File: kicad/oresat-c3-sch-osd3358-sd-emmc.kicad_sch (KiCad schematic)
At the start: 41 parts, among them J5 DM3BT-DSF-PEJS, U1 OSD3358-512M-BSM, U8 TCAN330, U9 EMMC+RESET+5.1-COMPATIBLE-BA

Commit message: Fixed test points; added RF test points. Started on layout and component packages for UHF radio.
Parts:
- TP23, TP24, TP26, TP27, TP31, TP32, TP37, TP38, TP39, TP40, TP42, TP46, TP47, TP48, TP49, TP50: footprint TestPoint:TestPoint_Pad_D1.0mm -> oresat-misc:TestPoint_Pad_D1.0mm
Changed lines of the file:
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@@
       (effects (font (size 1.27 1.27)) hide)
     )
-    (property "Footprint" "TestPoint:TestPoint_Pad_D1.0mm" (at 160.02 93.98 0)
+    (property "Footprint" "oresat-misc:TestPoint_Pad_D1.0mm" (at 160.02 93.98 0)
       (effects (font (size 1.27 1.27)) hide)
     )
@@
       (effects (font (size 1.27 1.27)) hide)
     )
-    (property "Footprint" "TestPoint:TestPoint_Pad_D1.0mm" (at 228.6 119.38 0)
+    (property "Footprint" "oresat-misc:TestPoint_Pad_D1.0mm" (at 228.6 119.38 0)
       (effects (font (size 1.27 1.27)) hide)
     )
@@
       (effects (font (size 1.27 1.27)) hide)
     )
-    (property "Footprint" "TestPoint:TestPoint_Pad_D1.0mm" (at 228.6 154.94 0)
+    (property "Footprint" "oresat-misc:TestPoint_Pad_D1.0mm" (at 228.6 154.94 0)
       (effects (font (size 1.27 1.27)) hide)
     )
@@
       (effects (font (size 1.27 1.27)) hide)
     )
-    (property "Footprint" "TestPoint:TestPoint_Pad_D1.0mm" (at 228.6 116.84 0)
+    (property "Footprint" "oresat-misc:TestPoint_Pad_D1.0mm" (at 228.6 116.84 0)
       (effects (font (size 1.27 1.27)) hide)
     )
@@
       (effects (font (size 1.27 1.27)) hide)
     )
-    (property "Footprint" "TestPoint:TestPoint_Pad_D1.0mm" (at 228.6 198.12 0)
+    (property "Footprint" "oresat-misc:TestPoint_Pad_D1.0mm" (at 228.6 198.12 0)
       (effects (font (size 1.27 1.27)) hide)
     )
@@
       (effects (font (size 1.27 1.27)) hide)
     )
-    (property "Footprint" "TestPoint:TestPoint_Pad_D1.0mm" (at 144.78 59.69 0)
+    (property "Footprint" "oresat-misc:TestPoint_Pad_D1.0mm" (at 144.78 59.69 0)
       (effects (font (size 1.27 1.27)) hide)
     )
@@
       (effects (font (size 1.27 1.27)) hide)
     )
-    (property "Footprint" "TestPoint:TestPoint_Pad_D1.0mm" (at 228.6 124.46 0)
+    (property "Footprint" "oresat-misc:TestPoint_Pad_D1.0mm" (at 228.6 124.46 0)
       (effects (font (size 1.27 1.27)) hide)
     )
@@
       (effects (font (size 1.27 1.27)) hide)
     )
-    (property "Footprint" "TestPoint:TestPoint_Pad_D1.0mm" (at 228.6 195.58 0)
+    (property "Footprint" "oresat-misc:TestPoint_Pad_D1.0mm" (at 228.6 195.58 0)
       (effects (font (size 1.27 1.27)) hide)
     )
@@
       (effects (font (size 1.27 1.27)) hide)
     )
-    (property "Footprint" "TestPoint:TestPoint_Pad_D1.0mm" (at 228.6 167.64 0)
+    (property "Footprint" "oresat-misc:TestPoint_Pad_D1.0mm" (at 228.6 167.64 0)
       (effects (font (size 1.27 1.27)) hide)
     )
@@
       (effects (font (size 1.27 1.27)) hide)
     )
-    (property "Footprint" "TestPoint:TestPoint_Pad_D1.0mm" (at 160.02 172.72 0)
+    (property "Footprint" "oresat-misc:TestPoint_Pad_D1.0mm" (at 160.02 172.72 0)
       (effects (font (size 1.27 1.27)) hide)
     )
@@
       (effects (font (size 1.27 1.27)) hide)
     )
-    (property "Footprint" "TestPoint:TestPoint_Pad_D1.0mm" (at 228.6 160.02 0)
+    (property "Footprint" "oresat-misc:TestPoint_Pad_D1.0mm" (at 228.6 160.02 0)
       (effects (font (size 1.27 1.27)) hide)
     )
@@
       (effects (font (size 1.27 1.27)) hide)
     )
-    (property "Footprint" "TestPoint:TestPoint_Pad_D1.0mm" (at 228.6 121.92 0)
+    (property "Footprint" "oresat-misc:TestPoint_Pad_D1.0mm" (at 228.6 121.92 0)
       (effects (font (size 1.27 1.27)) hide)
     )
@@
       (effects (font (size 1.27 1.27)) hide)
     )
-    (property "Footprint" "TestPoint:TestPoint_Pad_D1.0mm" (at 160.02 111.76 0)
+    (property "Footprint" "oresat-misc:TestPoint_Pad_D1.0mm" (at 160.02 111.76 0)
       (effects (font (size 1.27 1.27)) hide)
     )
@@
       (effects (font (size 1.27 1.27)) hide)
     )
-    (property "Footprint" "TestPoint:TestPoint_Pad_D1.0mm" (at 144.78 62.23 0)
+    (property "Footprint" "oresat-misc:TestPoint_Pad_D1.0mm" (at 144.78 62.23 0)
       (effects (font (size 1.27 1.27)) hide)
     )
@@
       (effects (font (size 1.27 1.27)) hide)
     )
-    (property "Footprint" "TestPoint:TestPoint_Pad_D1.0mm" (at 228.6 142.24 0)
+    (property "Footprint" "oresat-misc:TestPoint_Pad_D1.0mm" (at 228.6 142.24 0)
       (effects (font (size 1.27 1.27)) hide)
     )
@@
       (effects (font (size 1.27 1.27)) hide)
     )
-    (property "Footprint" "TestPoint:TestPoint_Pad_D1.0mm" (at 160.02 175.26 0)
-      (effects (font (size 1.27 1.27)) hide)
-    )
+    (property "Footprint" "oresat-misc:TestPoint_Pad_D1.0mm" (at 160.02 175.26 0)
+      (effects (font (size 1.27 1.27)) hide)
+    )

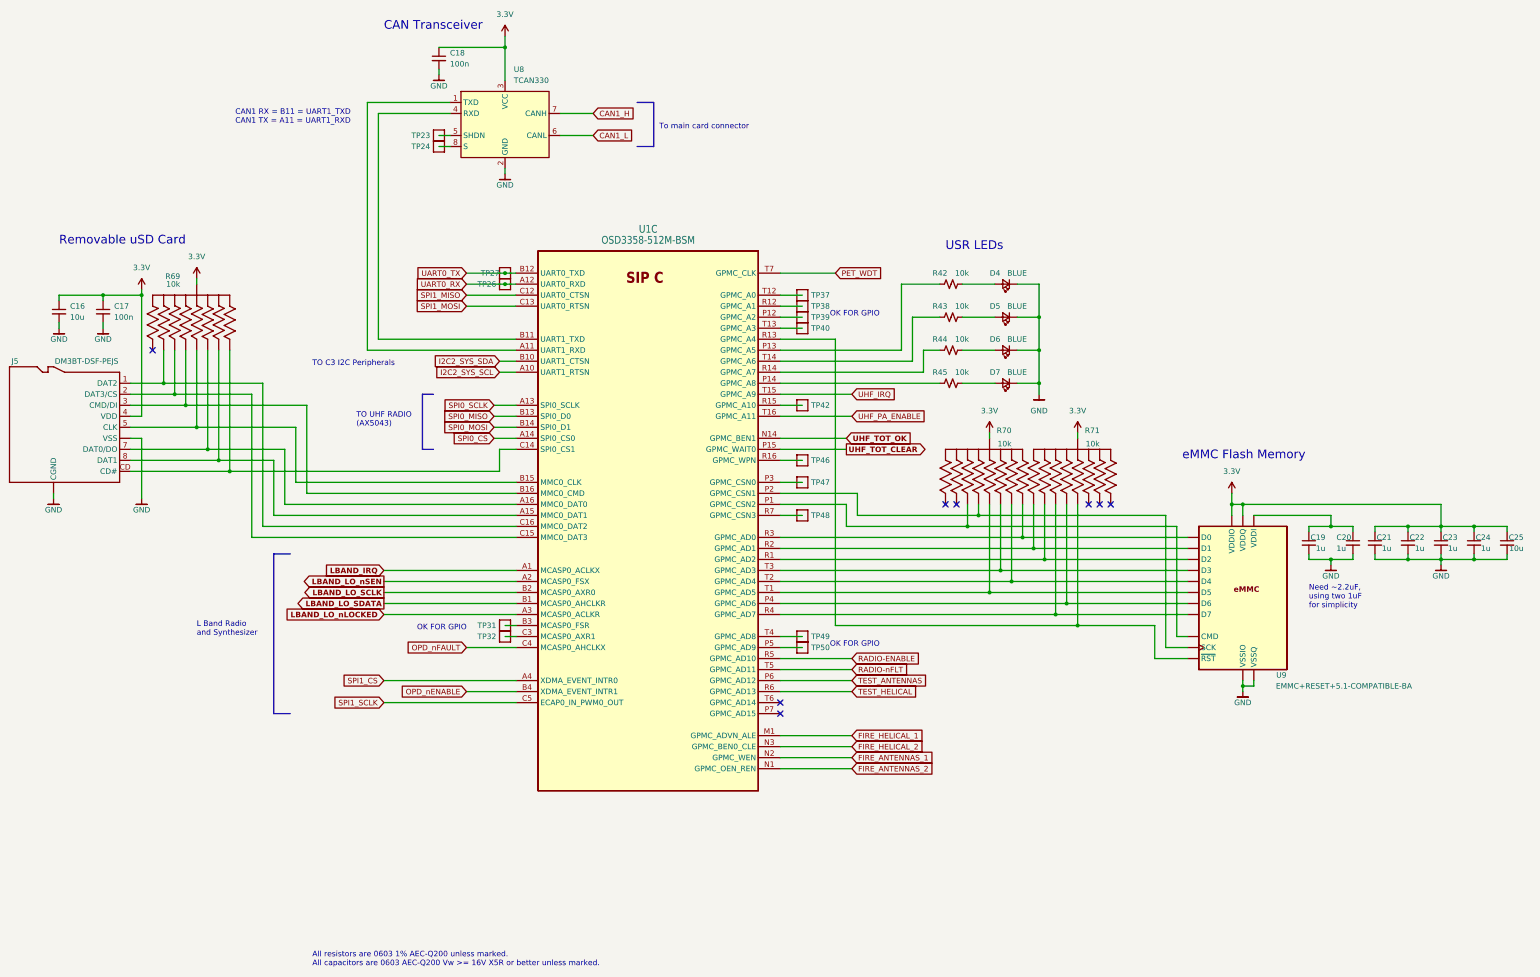
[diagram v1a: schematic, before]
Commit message: Fixed footprints and laid out WDT and OPD circuitry.
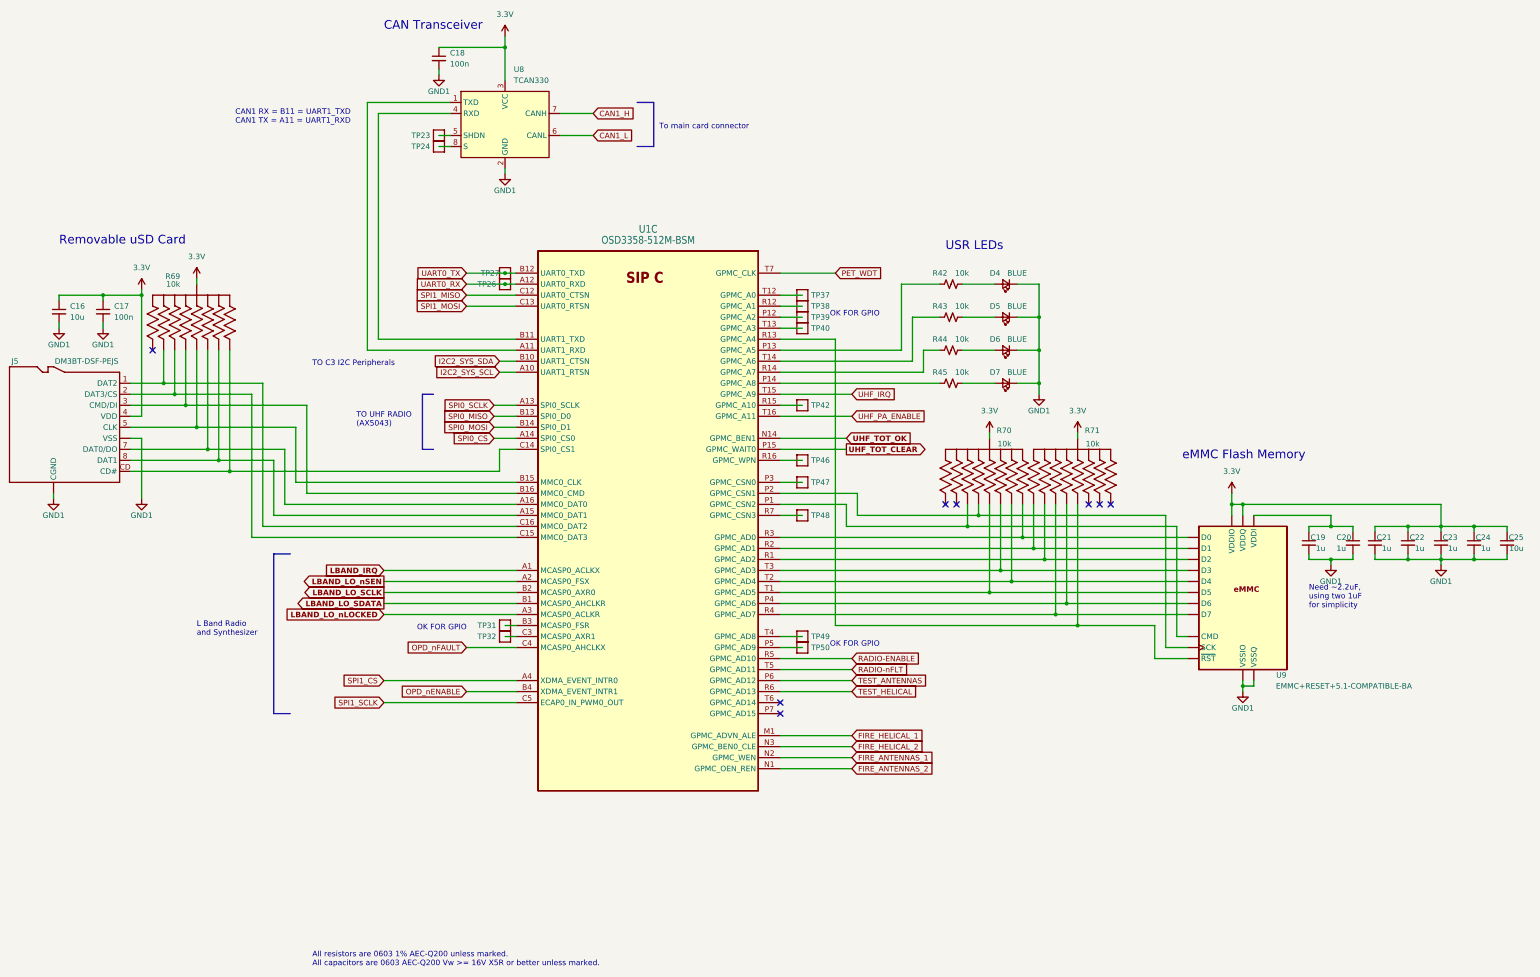
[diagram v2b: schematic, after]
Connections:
- net GND renamed GND1
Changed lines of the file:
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@@
     )
   )
-  (symbol (lib_id "oresat-power:GND") (at 375.92 168.91 0) (unit 1)
-    (in_bom yes) (on_board yes) (dnp no)
-    (property "Reference" "#GND0147" (at 375.92 175.26 0)
-      (effects (font (size 1.27 1.27)) hide)
-    )
-    (property "Value" "GND" (at 375.92 171.45 0)
+  (symbol (lib_id "power:GND1") (at 375.92 168.91 0) (unit 1)
+    (in_bom yes) (on_board yes) (dnp no)
+    (property "Reference" "#PWR0149" (at 375.92 175.26 0)
+      (effects (font (size 1.27 1.27)) hide)
+    )
+    (property "Value" "GND1" (at 375.92 172.72 0)
       (effects (font (size 1.27 1.27)))
     )
@@
       (project "oresat-c3"
         (path "/65d12cdd-c326-4033-9053-c59fa4e0b25e/f3d147ad-4cea-4d77-ae60-95882b03454e"
-          (reference "#GND0147") (unit 1)
+          (reference "#PWR0149") (unit 1)
         )
       )
@@
     )
   )
-  (symbol (lib_id "oresat-power:GND") (at 55.88 153.67 0) (unit 1)
-    (in_bom yes) (on_board yes) (dnp no)
-    (property "Reference" "#GND0138" (at 55.88 160.02 0)
-      (effects (font (size 1.27 1.27)) hide)
-    )
-    (property "Value" "GND" (at 55.88 156.21 0)
+  (symbol (lib_id "power:GND1") (at 55.88 153.67 0) (unit 1)
+    (in_bom yes) (on_board yes) (dnp no)
+    (property "Reference" "#PWR0155" (at 55.88 160.02 0)
+      (effects (font (size 1.27 1.27)) hide)
+    )
+    (property "Value" "GND1" (at 55.88 157.48 0)
       (effects (font (size 1.27 1.27)))
     )
@@
       (project "oresat-c3"
         (path "/65d12cdd-c326-4033-9053-c59fa4e0b25e/f3d147ad-4cea-4d77-ae60-95882b03454e"
-          (reference "#GND0138") (unit 1)
+          (reference "#PWR0155") (unit 1)
         )
       )
@@
     )
   )
-  (symbol (lib_id "oresat-power:GND") (at 283.21 129.54 0) (unit 1)
+  (symbol (lib_id "power:GND1") (at 283.21 129.54 0) (unit 1)
     (in_bom yes) (on_board yes) (dnp no) (fields_autoplaced)
-    (property "Reference" "#GND0150" (at 283.21 135.89 0)
-      (effects (font (size 1.27 1.27)) hide)
-    )
-    (property "Value" "GND" (at 283.21 133.35 0)
+    (property "Reference" "#PWR0148" (at 283.21 135.89 0)
+      (effects (font (size 1.27 1.27)) hide)
+    )
+    (property "Value" "GND1" (at 283.21 133.35 0)
       (effects (font (size 1.27 1.27)))
     )
@@
       (project "oresat-c3"
         (path "/65d12cdd-c326-4033-9053-c59fa4e0b25e/f3d147ad-4cea-4d77-ae60-95882b03454e"
-          (reference "#GND0150") (unit 1)
-        )
-      )
-    )
-  )
-  (symbol (lib_id "oresat-power:GND") (at 76.2 153.67 0) (unit 1)
-    (in_bom yes) (on_board yes) (dnp no)
-    (property "Reference" "#GND0139" (at 76.2 160.02 0)
-      (effects (font (size 1.27 1.27)) hide)
-    )
-    (property "Value" "GND" (at 76.2 156.21 0)
+          (reference "#PWR0148") (unit 1)
+        )
+      )
+    )
+  )
+  (symbol (lib_id "power:GND1") (at 76.2 153.67 0) (unit 1)
+    (in_bom yes) (on_board yes) (dnp no)
+    (property "Reference" "#PWR0156" (at 76.2 160.02 0)
+      (effects (font (size 1.27 1.27)) hide)
+    )
+    (property "Value" "GND1" (at 76.2 157.48 0)
       (effects (font (size 1.27 1.27)))
     )
@@
       (project "oresat-c3"
         (path "/65d12cdd-c326-4033-9053-c59fa4e0b25e/f3d147ad-4cea-4d77-ae60-95882b03454e"
-          (reference "#GND0139") (unit 1)
+          (reference "#PWR0156") (unit 1)
         )
       )
@@
     )
   )
-  (symbol (lib_id "oresat-power:GND") (at 350.52 168.91 0) (unit 1)
-    (in_bom yes) (on_board yes) (dnp no)
-    (property "Reference" "#GND0149" (at 350.52 175.26 0)
-      (effects (font (size 1.27 1.27)) hide)
-    )
-    (property "Value" "GND" (at 350.52 171.45 0)
+  (symbol (lib_id "power:GND1") (at 350.52 168.91 0) (unit 1)
+    (in_bom yes) (on_board yes) (dnp no)
+    (property "Reference" "#PWR0151" (at 350.52 175.26 0)
+      (effects (font (size 1.27 1.27)) hide)
+    )
+    (property "Value" "GND1" (at 350.52 172.72 0)
       (effects (font (size 1.27 1.27)))
     )
@@
       (project "oresat-c3"
         (path "/65d12cdd-c326-4033-9053-c59fa4e0b25e/f3d147ad-4cea-4d77-ae60-95882b03454e"
-          (reference "#GND0149") (unit 1)
-        )
-      )
-    )
-  )
-  (symbol (lib_id "oresat-power:GND") (at 57.15 114.3 0) (unit 1)
-    (in_bom yes) (on_board yes) (dnp no)
-    (property "Reference" "#GND0140" (at 57.15 120.65 0)
-      (effects (font (size 1.27 1.27)) hide)
-    )
-    (property "Value" "GND" (at 57.15 116.84 0)
+          (reference "#PWR0151") (unit 1)
+        )
+      )
+    )
+  )
+  (symbol (lib_id "power:GND1") (at 57.15 114.3 0) (unit 1)
+    (in_bom yes) (on_board yes) (dnp no)
+    (property "Reference" "#PWR0152" (at 57.15 120.65 0)
+      (effects (font (size 1.27 1.27)) hide)
+    )
+    (property "Value" "GND1" (at 57.15 118.11 0)
       (effects (font (size 1.27 1.27)))
     )
@@
       (project "oresat-c3"
         (path "/65d12cdd-c326-4033-9053-c59fa4e0b25e/f3d147ad-4cea-4d77-ae60-95882b03454e"
-          (reference "#GND0140") (unit 1)
+          (reference "#PWR0152") (unit 1)
         )
       )
@@
     )
   )
-  (symbol (lib_id "oresat-power:GND") (at 67.31 114.3 0) (unit 1)
-    (in_bom yes) (on_board yes) (dnp no)
-    (property "Reference" "#GND0141" (at 67.31 120.65 0)
-      (effects (font (size 1.27 1.27)) hide)
-    )
-    (property "Value" "GND" (at 67.31 116.84 0)
+  (symbol (lib_id "power:GND1") (at 67.31 114.3 0) (unit 1)
+    (in_bom yes) (on_board yes) (dnp no)
+    (property "Reference" "#PWR0153" (at 67.31 120.65 0)
+      (effects (font (size 1.27 1.27)) hide)
+    )
+    (property "Value" "GND1" (at 67.31 118.11 0)
       (effects (font (size 1.27 1.27)))
     )
@@
       (project "oresat-c3"
         (path "/65d12cdd-c326-4033-9053-c59fa4e0b25e/f3d147ad-4cea-4d77-ae60-95882b03454e"
-          (reference "#GND0141") (unit 1)
+          (reference "#PWR0153") (unit 1)
         )
       )
@@
     )
   )
-  (symbol (lib_id "oresat-power:GND") (at 160.02 78.74 0) (unit 1)
-    (in_bom yes) (on_board yes) (dnp no)
-    (property "Reference" "#GND0146" (at 160.02 85.09 0)
-      (effects (font (size 1.27 1.27)) hide)
-    )
-    (property "Value" "GND" (at 160.02 81.28 0)
+  (symbol (lib_id "power:GND1") (at 160.02 78.74 0) (unit 1)
+    (in_bom yes) (on_board yes) (dnp no)
+    (property "Reference" "#PWR0157" (at 160.02 85.09 0)
+      (effects (font (size 1.27 1.27)) hide)
+    )
+    (property "Value" "GND1" (at 160.02 82.55 0)
       (effects (font (size 1.27 1.27)))
     )
@@
       (project "oresat-c3"
         (path "/65d12cdd-c326-4033-9053-c59fa4e0b25e/f3d147ad-4cea-4d77-ae60-95882b03454e"
-          (reference "#GND0146") (unit 1)
+          (reference "#PWR0157") (unit 1)
         )
       )
@@
     )
   )
-  (symbol (lib_id "oresat-power:GND") (at 330.2 198.12 0) (unit 1)
-    (in_bom yes) (on_board yes) (dnp no)
-    (property "Reference" "#GND0148" (at 330.2 204.47 0)
-      (effects (font (size 1.27 1.27)) hide)
-    )
-    (property "Value" "GND" (at 330.2 200.66 0)
+  (symbol (lib_id "power:GND1") (at 330.2 198.12 0) (unit 1)
+    (in_bom yes) (on_board yes) (dnp no)
+    (property "Reference" "#PWR0150" (at 330.2 204.47 0)
+      (effects (font (size 1.27 1.27)) hide)
+    )
+    (property "Value" "GND1" (at 330.2 201.93 0)
       (effects (font (size 1.27 1.27)))
     )
@@
       (project "oresat-c3"
         (path "/65d12cdd-c326-4033-9053-c59fa4e0b25e/f3d147ad-4cea-4d77-ae60-95882b03454e"
-          (reference "#GND0148") (unit 1)
-        )
-      )
-    )
-  )
-  (symbol (lib_id "oresat-power:GND") (at 144.78 55.88 0) (unit 1)
-    (in_bom yes) (on_board yes) (dnp no)
-    (property "Reference" "#GND0145" (at 144.78 62.23 0)
-      (effects (font (size 1.27 1.27)) hide)
-    )
-    (property "Value" "GND" (at 144.78 58.42 0)
+          (reference "#PWR0150") (unit 1)
+        )
+      )
+    )
+  )
+  (symbol (lib_id "power:GND1") (at 144.78 55.88 0) (unit 1)
+    (in_bom yes) (on_board yes) (dnp no)
+    (property "Reference" "#PWR0154" (at 144.78 62.23 0)
+      (effects (font (size 1.27 1.27)) hide)
+    )
+    (property "Value" "GND1" (at 144.78 59.69 0)
       (effects (font (size 1.27 1.27)))
     )
@@
       (project "oresat-c3"
         (path "/65d12cdd-c326-4033-9053-c59fa4e0b25e/f3d147ad-4cea-4d77-ae60-95882b03454e"
-          (reference "#GND0145") (unit 1)
-        )
-      )
+          (reference "#PWR0154") (unit 1)
+        )
+      )

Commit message: More progress on C3 v6. All ICs and Packages are in, deployer and power supply and I2C subsystems laid out.
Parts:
- U9: footprint oresat-live-card:BGA-153(11.5X13)(EMMC-BA) -> oresat-ics:BGA-153(11.5X13)(EMMC-BA)
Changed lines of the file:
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@@
       (effects (font (size 1.27 1.27)) (justify left))
     )
-    (property "Footprint" "oresat-live-card:BGA-153(11.5X13)(EMMC-BA)" (at 330.2 175.26 0)
+    (property "Footprint" "oresat-ics:BGA-153(11.5X13)(EMMC-BA)" (at 330.2 175.26 0)
       (effects (font (size 1.27 1.27)) hide)
     )
